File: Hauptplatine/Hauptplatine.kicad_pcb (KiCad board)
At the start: 2 copper layers, 179.7 x 194.9 mm, 47 parts, among them IC1 74HC4040, IC10 74HC02, IC12 Arduino_Nano_v2.x, IC2 74HC4040, IC20 74HC04, IC21 74HC390, IC22 74HC390, IC23 74HC390, IC24 74HC390, IC25 74HC107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

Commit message: Short break in reset
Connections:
- IC12 pad 28: VCC -> unconnected-(IC12-Pad28)
- IC12 pad 3: VCC -> unconnected-(IC12-Pad3)
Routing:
- net VCC: track 1897.4 -> 1869.6 mm
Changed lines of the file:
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@@
   (net 153 "RESET_FF")
   (net 154 "Net-(IC20-Pad6)")
+  (net 155 "unconnected-(IC12-Pad3)")
+  (net 156 "unconnected-(IC12-Pad28)")
   (footprint "Connector_PinSocket_2.54mm:PinSocket_1x10_P2.54mm_Vertical" (layer "F.Cu")
     (at 112.395 168.91 90)
@@
       (net 120 "unconnected-(IC12-Pad2)") (pinfunction "D0/RX") (pintype "bidirectional+no_connect"))
     (pad "3" thru_hole oval (at 0 5.08 90) (size 1.6 1.6) (drill 1) (layers *.Cu *.Mask)
-      (net 1 "VCC") (pinfunction "~{RESET}") (pintype "input"))
+      (net 155 "unconnected-(IC12-Pad3)") (pinfunction "~{RESET}") (pintype "input+no_connect"))
     (pad "4" thru_hole oval (at 0 7.62 90) (size 1.6 1.6) (drill 1) (layers *.Cu *.Mask)
       (net 2 "GND") (pinfunction "GND") (pintype "power_in"))
@@
       (net 107 "unconnected-(IC12-Pad27)") (pinfunction "+5V") (pintype "power_out+no_connect"))
     (pad "28" thru_hole oval (at 15.24 5.08 90) (size 1.6 1.6) (drill 1) (layers *.Cu *.Mask)
-      (net 1 "VCC") (pinfunction "~{RESET}") (pintype "input"))
+      (net 156 "unconnected-(IC12-Pad28)") (pinfunction "~{RESET}") (pintype "input+no_connect"))
     (pad "29" thru_hole oval (at 15.24 2.54 90) (size 1.6 1.6) (drill 1) (layers *.Cu *.Mask)
       (net 2 "GND") (pinfunction "GND") (pintype "power_in"))
@@
   (segment (start 24.765 104.14) (end 24.765 53.975) (width 4) (layer "F.Cu") (net 1))
   (segment (start 95.2348 20.64) (end 95.25 20.6552) (width 1) (layer "F.Cu") (net 1))
-  (segment (start 167.01 9.53) (end 165.735 8.255) (width 1) (layer "F.Cu") (net 1))
-  (segment (start 173.35 10.155) (end 171.45 8.255) (width 1) (layer "F.Cu") (net 1))
   (segment (start 115.57 109.855) (end 146.685 109.855) (width 1) (layer "F.Cu") (net 1))
   (segment (start 146.685 99.06) (end 127.635 80.01) (width 4) (layer "F.Cu") (net 1))
@@
   (segment (start 73.025 128.905) (end 72.705 129.225) (width 1) (layer "F.Cu") (net 1))
   (segment (start 34.036 129.159) (end 71.511 129.159) (width 1) (layer "F.Cu") (net 1))
+  (segment (start 152.4 8.255) (end 157.48 8.255) (width 4) (layer "F.Cu") (net 1))
   (segment (start 127.635 74.295) (end 127.635 53.975) (width 4) (layer "F.Cu") (net 1))
-  (segment (start 158.75 16.51) (end 158.75 8.89) (width 1) (layer "F.Cu") (net 1))
   (segment (start 127.32 73.98) (end 127.635 74.295) (width 1) (layer "F.Cu") (net 1))
   (segment (start 25.4 24.765) (end 36.83 24.765) (width 4) (layer "F.Cu") (net 1))
@@
   (segment (start 81.28 34.29) (end 81.28 36.83) (width 1) (layer "F.Cu") (net 1))
   (segment (start 44.13 20.64) (end 37.78 20.64) (width 1) (layer "F.Cu") (net 1))
-  (segment (start 173.35 11.43) (end 173.35 10.155) (width 1) (layer "F.Cu") (net 1))
   (segment (start 73.025 126.365) (end 73.025 128.905) (width 1) (layer "F.Cu") (net 1))
   (segment (start 127.635 80.01) (end 127.635 74.295) (width 4) (layer "F.Cu") (net 1))
+  (segment (start 157.48 8.255) (end 159.385 8.255) (width 4) (layer "F.Cu") (net 1))
   (segment (start 44.13 20.64) (end 95.2348 20.64) (width 1) (layer "F.Cu") (net 1))
   (segment (start 36.83 8.89) (end 37.465 8.255) (width 4) (layer "F.Cu") (net 1))
@@
   (segment (start 113.98 73.98) (end 110.17 73.98) (width 1) (layer "F.Cu") (net 1))
   (segment (start 32.705 37.15) (end 25.08 37.15) (width 1) (layer "F.Cu") (net 1))
+  (segment (start 156.845 8.89) (end 157.48 8.255) (width 1) (layer "F.Cu") (net 1))
   (segment (start 132.08 196.85) (end 193.675 196.85) (width 4) (layer "F.Cu") (net 1))
   (segment (start 60.325 107.315) (end 60.325 109.855) (width 1) (layer "F.Cu") (net 1))
@@
   (segment (start 32.385 128.905) (end 26.035 128.905) (width 1) (layer "F.Cu") (net 1))
   (segment (start 34.29 128.905) (end 34.036 129.159) (width 1) (layer "F.Cu") (net 1))
-  (segment (start 152.4 8.255) (end 159.385 8.255) (width 4) (layer "F.Cu") (net 1))
   (segment (start 60.325 109.855) (end 87.63 109.855) (width 1) (layer "F.Cu") (net 1))
   (segment (start 146.685 129.54) (end 146.37 129.225) (width 1) (layer "F.Cu") (net 1))
@@
   (segment (start 98.425 73.66) (end 100.965 73.66) (width 1) (layer "B.Cu") (net 1))
   (segment (start 51.435 78.74) (end 51.435 76.835) (width 1) (layer "B.Cu") (net 1))
-  (segment (start 158.75 31.75) (end 158.75 16.51) (width 1) (layer "B.Cu") (net 1))
   (segment (start 51.435 76.835) (end 54.61 73.66) (width 1) (layer "B.Cu") (net 1))
   (segment (start 70.485 133.985) (end 70.485 126.365) (width 1) (layer "B.Cu") (net 1))

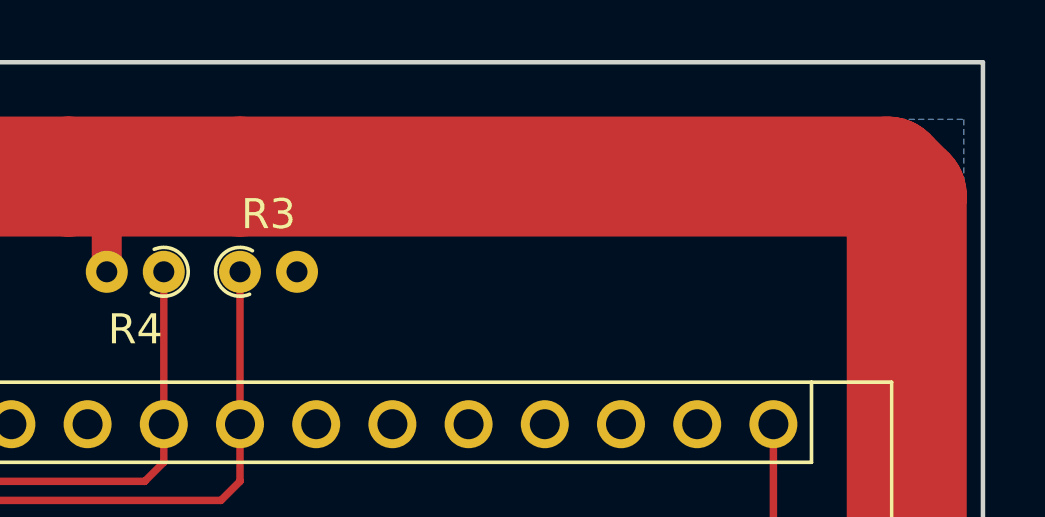
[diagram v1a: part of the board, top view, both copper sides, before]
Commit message: Reset Logic updated
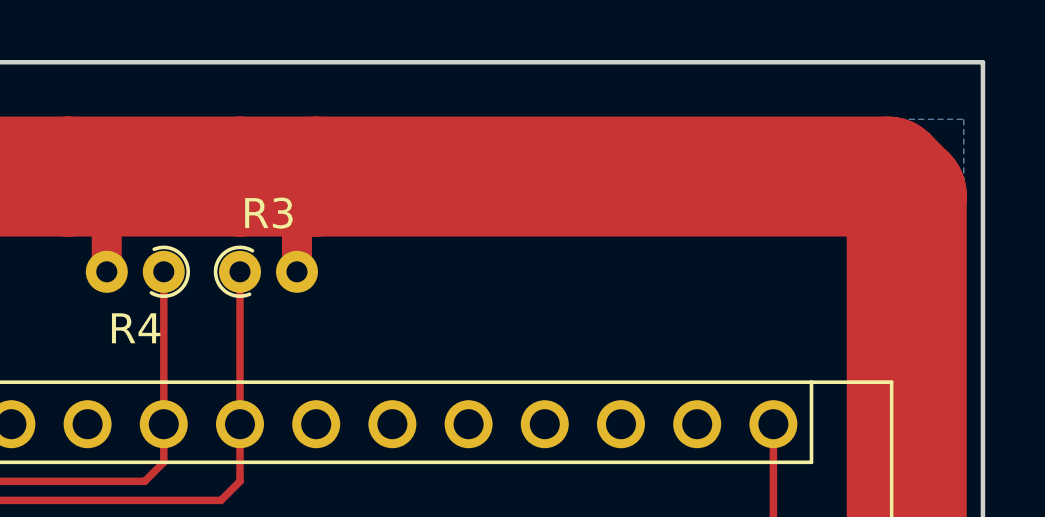
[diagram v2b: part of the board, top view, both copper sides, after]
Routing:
- net VCC: track 1869.6 -> 1873.1 mm
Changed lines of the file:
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@@
   (segment (start 146.37 129.225) (end 114.615 129.225) (width 1) (layer "F.Cu") (net 1))
   (segment (start 90.805 128.905) (end 90.485 129.225) (width 1) (layer "F.Cu") (net 1))
-  (segment (start 171.45 8.255) (end 193.04 8.255) (width 4) (layer "F.Cu") (net 1))
   (segment (start 69.215 73.66) (end 69.535 73.98) (width 1) (layer "F.Cu") (net 1))
   (segment (start 57.15 34.29) (end 57.15 36.835) (width 1) (layer "F.Cu") (net 1))
@@
   (segment (start 182.88 114.935) (end 183.515 114.3) (width 2.5) (layer "F.Cu") (net 1))
   (segment (start 69.215 71.12) (end 69.215 73.66) (width 1) (layer "F.Cu") (net 1))
+  (segment (start 173.35 11.43) (end 173.35 8.895) (width 1) (layer "F.Cu") (net 1))
   (segment (start 33.02 36.835) (end 32.705 37.15) (width 1) (layer "F.Cu") (net 1))
   (segment (start 24.765 53.975) (end 24.765 49.53) (width 4) (layer "F.Cu") (net 1))
   (segment (start 114.935 107.315) (end 114.935 109.22) (width 1) (layer "F.Cu") (net 1))
   (segment (start 159.385 8.255) (end 165.735 8.255) (width 4) (layer "F.Cu") (net 1))
+  (segment (start 173.99 8.255) (end 193.04 8.255) (width 4) (layer "F.Cu") (net 1))
   (segment (start 56.515 73.66) (end 56.835 73.98) (width 1) (layer "F.Cu") (net 1))
   (segment (start 73.66 17.78) (end 73.66 20.32) (width 1) (layer "F.Cu") (net 1))
@@
   (segment (start 82.55 50.8) (end 82.55 53.345) (width 1) (layer "F.Cu") (net 1))
   (segment (start 70.485 126.365) (end 70.485 128.905) (width 1) (layer "F.Cu") (net 1))
+  (segment (start 173.35 8.895) (end 173.99 8.255) (width 1) (layer "F.Cu") (net 1))
   (segment (start 36.83 21.59) (end 36.83 8.89) (width 4) (layer "F.Cu") (net 1))
   (segment (start 73.025 128.905) (end 72.705 129.225) (width 1) (layer "F.Cu") (net 1))
@@
   (segment (start 99.695 50.8) (end 99.695 53.34) (width 1) (layer "F.Cu") (net 1))
   (segment (start 70.805 129.225) (end 70.739 129.159) (width 1) (layer "F.Cu") (net 1))
+  (segment (start 171.45 8.255) (end 173.99 8.255) (width 4) (layer "F.Cu") (net 1))
   (segment (start 134.62 196.85) (end 25.4 196.85) (width 4) (layer "F.Cu") (net 1))
   (via (at 117.475 139.065) (size 1) (drill 0.6) (layers "F.Cu" "B.Cu") (net 1))

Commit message: Updated
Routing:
- net GND: track 1008.3 -> 1056.0 mm
- net 0.5HZ: track 210.1 -> 217.9 mm
- net RESET_COUNTER: track 320.2 -> 327.5 mm
- net DONE: track 161.9 -> 166.4 mm
- net SDA: track 307.5 -> 312.0 mm
- net _RESET_PERIOD: track 160.9 -> 164.2 mm
- net RESET_0.5HZ: track 232.3 -> 234.3 mm
- net VCC: track 1873.1 -> 1871.1 mm
